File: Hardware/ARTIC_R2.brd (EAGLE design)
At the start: 22.9 x 50.8 mm, 96 parts, among them J1 U.FL, J2 THING_PLUS, Q1 20V/4.2A/52mΩ/1.4W, U1 32M SPI Flash, U2 1.8V/100mA, U3 ARTIC_R2, U4 RFPA0133, U5 AS179-92LF, U6 DUAL-OPTOISOLATOR_SOIC8, X1 CRYSTAL-TCXO-26MHZ

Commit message: Nearing completion
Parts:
- added D3: RED, SparkFun-LED:LED-0603
- added JP5: JUMPER-SMT_2_NC_TRACE_SILK, SparkFun-Jumpers:SMT-JUMPER_2_NC_TRACE_SILK
- added R15: 1k, SparkFun-Resistors:0402-TIGHT
- added SPARKX1, SPARKX2: SPARKX-LOGO4, SparkX:SPARKX-MEDIUM
- added U$1: (no value), output:#TX#0
- added U$10: (no value), output:#CIPO0
- added U$11: (no value), output:#COPI0
- added U$12: (no value), output:COPI#0
- added U$13: (no value), output:#SCLK0
- added U$14: (no value), output:SCLK#0
- added U$15: (no value), output:#CS0
- added U$16: (no value), output:CS#0
- added U$17: (no value), output:GND#0
- added U$18: (no value), output:#RESETB0
- added U$19: (no value), output:#PWR_EN0
- added U$2: (no value), output:#RX#0
- added U$20: (no value), output:G8#0
- added U$21: (no value), output:#G80
- added U$22: (no value), output:G16#0
- added U$23: (no value), output:#G160
- added U$24: (no value), output:#BOOT0
- added U$25: (no value), output:#INT10
- added U$26: (no value), output:#INT20
- added U$27: (no value), output:#PWR_LED#0
- added U$28: (no value), output:#PWR#0
- added U$29: (no value), output:ARTIC_R2_BREAKOUT0
- added U$3: (no value), output:#RX_LED#0
- added U$4: (no value), output:#TX_LED#0
- added U$5, U$6: (no value), output:#3#3V#0
- added U$7, U$8: (no value), output:#1#8V#0
- added U$9: (no value), output:CIPO#0
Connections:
- new net N$37: D3.A, R15.1
- new net N$38: D3.C, JP5.2
- net BOOT: now also J2.5
- net G16: now also J2.4
- net G8: now also J2.3
- net GND: now also JP5.1
- net INT1: now also J2.6
- net INT2: now also J2.7
- net PWR_EN: now also J2.9
- net RESETB: now also J2.8
- net VDD: now also R15.2
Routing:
- net PWR_EN: track 1.41 -> 26.5 mm
- net BOOT: track 3.34 -> 23.2 mm, vias 0 -> 1
- net INT1: track 1.59 -> 19.9 mm
- net INT2: track 0.82 -> 18.0 mm
- net RESETB: track 3.62 -> 18.3 mm, vias 0 -> 1
- net G16: track 0.00 -> 6.88 mm
- net G8: track 0.00 -> 6.41 mm
- net N$37: track 0.00 -> 5.35 mm, vias 0 -> 2
- net N$38: track 0.00 -> 2.54 mm, vias 0 -> 1
- net GND: track 77.1 -> 79.4 mm, vias 166 -> 168
- net VDD: track 82.0 -> 83.6 mm
- net PA_PD: track 26.1 -> 26.9 mm
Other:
- board text added: "15"
- board text added: "2"
- board text added: "BOT"
- board text added: "TOP"
- board text added: "X01"

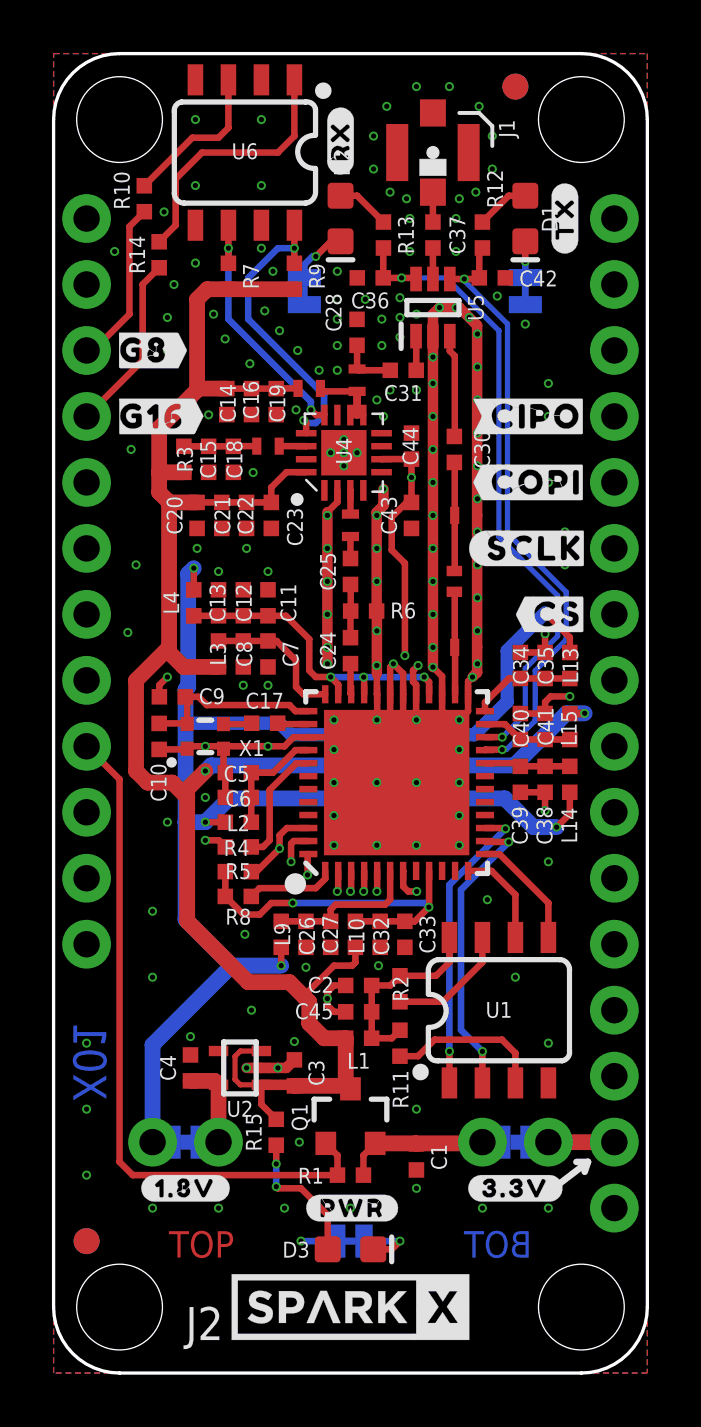
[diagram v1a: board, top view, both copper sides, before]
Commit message: Adjusted the RF track widths
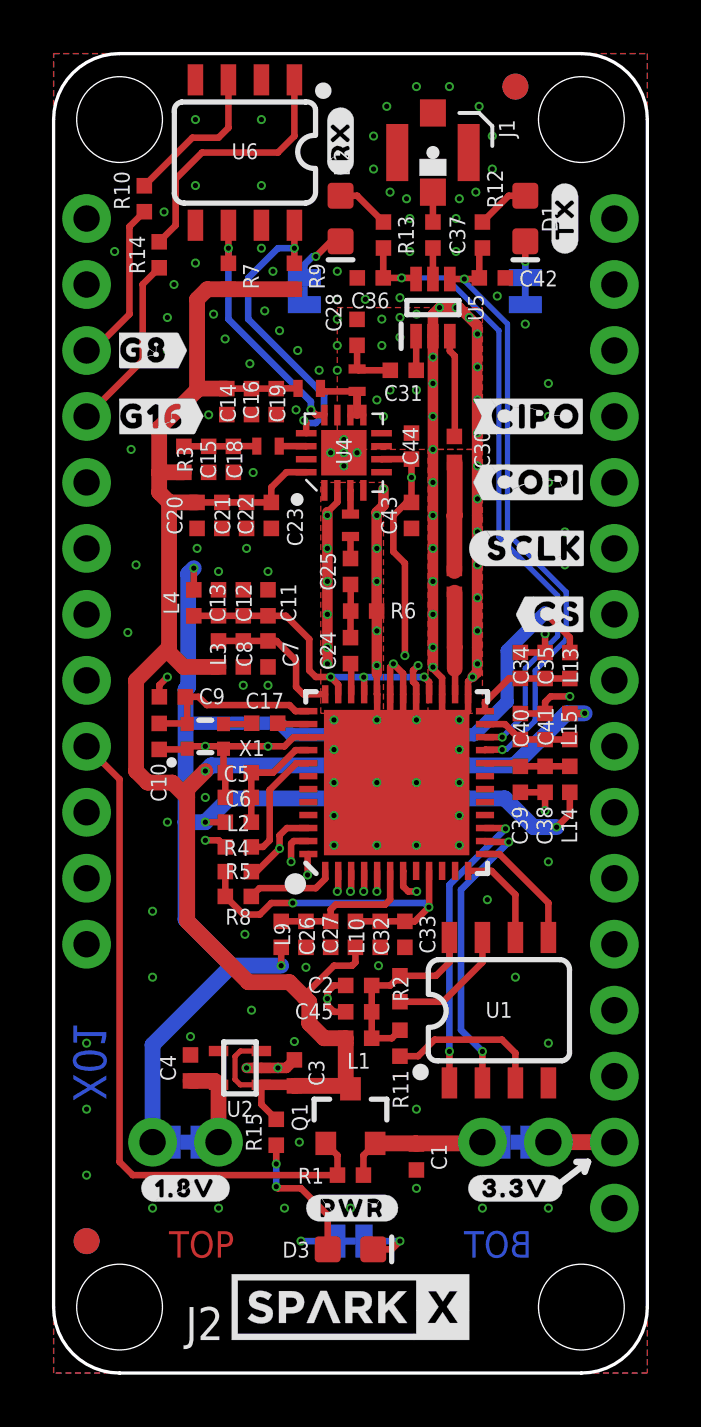
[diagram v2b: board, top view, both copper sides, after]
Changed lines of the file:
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@@
 <text x="13.97" y="4.445" size="1.016" layer="15" ratio="15">15</text>
 <text x="18.415" y="4.445" size="1.016" layer="16" ratio="15" rot="MR0">BOT</text>
+<wire x1="11.303" y1="32.639" x2="11.557" y2="32.639" width="0.254" layer="41"/>
 </plain>
 <attributes>
@@
 </element>
 <element name="X1" library="New_Parts_Clocks" package="CRYSTAL-TCXO-SMD-1.65X1.25" value="CRYSTAL-TCXO-26MHZ" x="5.842" y="24.511" smashed="yes">
+<attribute name="MOUSER_PART" value="449-LFTCXO073004CUTT" x="5.842" y="24.511" size="1.778" layer="27" display="off"/>
 <attribute name="NAME" x="7.128" y="23.756" size="0.6096" layer="25" font="vector" ratio="20"/>
+<attribute name="PROD_ID" value="" x="5.842" y="24.511" size="1.778" layer="27" display="off"/>
 </element>
 <element name="C9" library="SparkFun-Capacitors" package="0402-TIGHT" value="1.0uF" x="4.572" y="26.035" smashed="yes" rot="R180">
@@
 </element>
 <element name="R6" library="New_Parts_Resistors" package="0402-TIGHT" value="220OHM" x="11.938" y="29.337" smashed="yes" rot="R180">
+<attribute name="MOUSER_PART" value="755-SFR01MZPF2200" x="11.938" y="29.337" size="1.778" layer="27" rot="R180" display="off"/>
 <attribute name="NAME" x="13.462" y="29.664" size="0.6096" layer="25" font="vector" ratio="20" rot="R180" align="bottom-center"/>
 <attribute name="PROD_ID" value="" x="11.938" y="29.337" size="1.778" layer="27" rot="R180" display="off"/>
@@
 </element>
 <element name="R3" library="New_Parts_Resistors" package="0402-TIGHT" value="3.9OHM" x="5.0165" y="35.179" smashed="yes" rot="R270">
+<attribute name="MOUSER_PART" value="603-RC0402FR-073R9L" x="5.0165" y="35.179" size="1.778" layer="27" rot="R270" display="off"/>
 <attribute name="NAME" x="4.753" y="35.179" size="0.6096" layer="25" font="vector" ratio="20" rot="R270" align="bottom-center"/>
 <attribute name="PROD_ID" value="" x="5.0165" y="35.179" size="1.778" layer="27" ratio="15" rot="R270" display="off"/>
@@
 <contactref element="C38" pad="2"/>
 <via x="16.129" y="26.797" extent="1-16" drill="0.2"/>
-<wire x1="14.958" y1="26.133" x2="14.958" y2="26.825" width="0.254" layer="1"/>
+<wire x1="14.958" y1="26.133" x2="14.958" y2="26.7615" width="0.254" layer="1"/>
 <wire x1="14.605" y1="27.178" x2="14.605" y2="39.921" width="0.4064" layer="1"/>
-<wire x1="14.958" y1="26.825" x2="14.605" y2="27.178" width="0.254" layer="1"/>
+<wire x1="14.958" y1="26.7615" x2="14.605" y2="27.1145" width="0.254" layer="1"/>
+<wire x1="14.605" y1="27.1145" x2="14.605" y2="27.178" width="0.254" layer="1"/>
 <via x="14.605" y="27.178" extent="1-16" drill="0.2"/>
 <via x="14.605" y="31.75" extent="1-16" drill="0.2"/>
@@
 <vertex x="14.859" y="27.178"/>
 </polygon>
-<polygon width="0.254" layer="1" isolate="0.3048">
+<polygon width="0.254" layer="1" isolate="0.254" rank="3">
 <vertex x="0" y="50.8"/>
 <vertex x="22.86" y="50.8"/>
@@
 <vertex x="0" y="0"/>
 </polygon>
-<polygon width="0.254" layer="2" isolate="0.3048">
+<polygon width="0.254" layer="2" isolate="0.254" rank="2">
 <vertex x="0" y="50.8"/>
 <vertex x="22.86" y="50.8"/>
@@
 <vertex x="0" y="0"/>
 </polygon>
-<polygon width="0.254" layer="15" isolate="0.3048">
+<polygon width="0.254" layer="15" isolate="0.254" rank="2">
 <vertex x="0" y="50.8"/>
 <vertex x="22.86" y="50.8"/>
@@
 <vertex x="0" y="0"/>
 </polygon>
-<polygon width="0.254" layer="16" isolate="0.3048">
+<polygon width="0.254" layer="16" isolate="0.254" rank="2">
 <vertex x="0" y="50.8"/>
 <vertex x="22.86" y="50.8"/>
@@
 <wire x1="10.9093" y1="5.08" x2="9.525" y2="5.08" width="0.254" layer="16"/>
 <via x="9.525" y="5.08" extent="1-16" drill="0.2"/>
+<polygon width="0.1524" layer="1" isolate="0.127">
+<vertex x="10.287" y="34.29"/>
+<vertex x="12.7" y="34.29"/>
+<vertex x="12.7" y="25.4"/>
+<vertex x="10.287" y="25.4"/>
+</polygon>
+<polygon width="0.1524" layer="1" isolate="0.0762" rank="2">
+<vertex x="14.4145" y="35.56"/>
+<vertex x="16.51" y="35.56"/>
+<vertex x="16.51" y="25.4"/>
+<vertex x="14.4145" y="25.4"/>
+</polygon>
+<polygon width="0.1524" layer="1" isolate="0.127">
+<vertex x="10.922" y="41.021"/>
+<vertex x="16.51" y="41.021"/>
+<vertex x="16.51" y="35.56"/>
+<vertex x="10.922" y="35.56"/>
+</polygon>
 </signal>
 <signal name="EDAP">
@@
 <contactref element="C29" pad="P$2"/>
 <contactref element="L12" pad="P$2"/>
-<wire x1="15.4432" y1="33.02" x2="15.4432" y2="30.8927" width="0.254" layer="1"/>
 <wire x1="15.4432" y1="30.8927" x2="15.4305" y2="30.88" width="0.254" layer="1"/>
-<wire x1="15.4432" y1="33.02" x2="15.4432" y2="35.0473" width="0.254" layer="1"/>
 <wire x1="15.4432" y1="35.0473" x2="15.4305" y2="35.06" width="0.254" layer="1"/>
+<wire x1="15.4305" y1="30.88" x2="15.4305" y2="33.0073" width="0.6096" layer="1"/>
+<wire x1="15.4305" y1="33.0073" x2="15.4432" y2="33.02" width="0.6096" layer="1"/>
+<wire x1="15.4432" y1="33.02" x2="15.4432" y2="35.0473" width="0.6096" layer="1"/>
 </signal>
 <signal name="ANTENNA">
@@
 <wire x1="13.7795" y1="33.52" x2="13.7795" y2="34.4805" width="0.254" layer="1"/>
 <wire x1="13.7795" y1="33.52" x2="13.589" y2="33.52" width="0.254" layer="1"/>
-<wire x1="13.589" y1="33.52" x2="13.0175" y2="32.9485" width="0.254" layer="1"/>
+<wire x1="13.589" y1="33.52" x2="13.081" y2="33.012" width="0.254" layer="1"/>
 <wire x1="13.5255" y1="31.1785" x2="13.5255" y2="27.6225" width="0.254" layer="1"/>
 <via x="13.5255" y="27.6225" extent="1-16" drill="0.2"/>
-<wire x1="13.0175" y1="32.9485" x2="13.0175" y2="31.6865" width="0.254" layer="1"/>
-<wire x1="13.0175" y1="31.6865" x2="13.5255" y2="31.1785" width="0.254" layer="1"/>
+<wire x1="13.081" y1="33.012" x2="13.081" y2="31.623" width="0.254" layer="1"/>
+<wire x1="13.081" y1="31.623" x2="13.5255" y2="31.1785" width="0.254" layer="1"/>
 <wire x1="13.5255" y1="27.6225" x2="13.5255" y2="22.225" width="0.2032" layer="15"/>
-<wire x1="13.5255" y1="22.225" x2="12.1285" y2="20.828" width="0.2032" layer="15"/>
+<wire x1="13.5255" y1="22.225" x2="12.0015" y2="20.701" width="0.2032" layer="15"/>
 <wire x1="10.4775" y1="18.034" x2="11.43" y2="17.0815" width="0.2032" layer="15"/>
 <wire x1="11.43" y1="17.0815" x2="13.1445" y2="17.0815" width="0.2032" layer="15"/>
@@
 <wire x1="13.9795" y1="17.9165" x2="13.9795" y2="18.542" width="0.2032" layer="15"/>
 <wire x1="13.1445" y1="17.0815" x2="13.9795" y2="17.9165" width="0.2032" layer="15"/>
-<wire x1="12.1285" y1="20.828" x2="12.0015" y2="20.701" width="0.2032" layer="15"/>
 <wire x1="12.0015" y1="19.2405" x2="11.7475" y2="18.9865" width="0.2032" layer="15"/>
 <wire x1="10.7315" y1="18.9865" x2="10.4775" y2="18.7325" width="0.2032" layer="15"/>
@@
 <contactref element="U3" pad="34"/>
 <contactref element="C24" pad="1"/>
-<wire x1="11.458" y1="26.133" x2="11.43" y2="26.161" width="0.254" layer="1"/>
-<wire x1="11.43" y1="26.161" x2="11.43" y2="27.313" width="0.254" layer="1"/>
+<wire x1="11.458" y1="26.133" x2="11.458" y2="27.285" width="0.254" layer="1"/>
+<wire x1="11.458" y1="27.285" x2="11.43" y2="27.313" width="0.254" layer="1"/>
 </signal>
 <signal name="N$18">
@@
 <contactref element="L11" pad="P$2"/>
 <contactref element="C29" pad="P$1"/>
-<wire x1="15.458" y1="26.133" x2="15.458" y2="27.9252" width="0.254" layer="1"/>
+<wire x1="15.4432" y1="30.0673" x2="15.4305" y2="30.08" width="0.254" layer="1"/>
+<wire x1="15.4305" y1="30.0546" x2="15.4432" y2="30.0673" width="0.254" layer="1"/>
 <wire x1="15.458" y1="27.9252" x2="15.4432" y2="27.94" width="0.254" layer="1"/>
-<wire x1="15.4432" y1="27.94" x2="15.4432" y2="30.0673" width="0.254" layer="1"/>
-<wire x1="15.4432" y1="30.0673" x2="15.4305" y2="30.08" width="0.254" layer="1"/>
+<wire x1="15.4432" y1="30.0419" x2="15.44005" y2="30.04505" width="0.254" layer="1"/>
+<wire x1="15.44005" y1="30.04505" x2="15.4305" y2="30.0546" width="0.254" layer="1"/>
+<wire x1="15.4432" y1="27.94" x2="15.44005" y2="27.94760625" width="0.254" layer="1" curve="-45"/>
+<wire x1="15.4432" y1="27.1145" x2="15.4432" y2="27.94" width="0.6096" layer="1"/>
+<wire x1="15.458" y1="26.133" x2="15.458" y2="27.0997" width="0.254" layer="1"/>
+<wire x1="15.458" y1="27.0997" x2="15.4432" y2="27.1145" width="0.254" layer="1"/>
+<wire x1="15.44005" y1="27.94760625" x2="15.44005" y2="30.04505" width="0.6096" layer="1"/>
 </signal>
 <signal name="N$22">

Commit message: Added 4x4 test panel
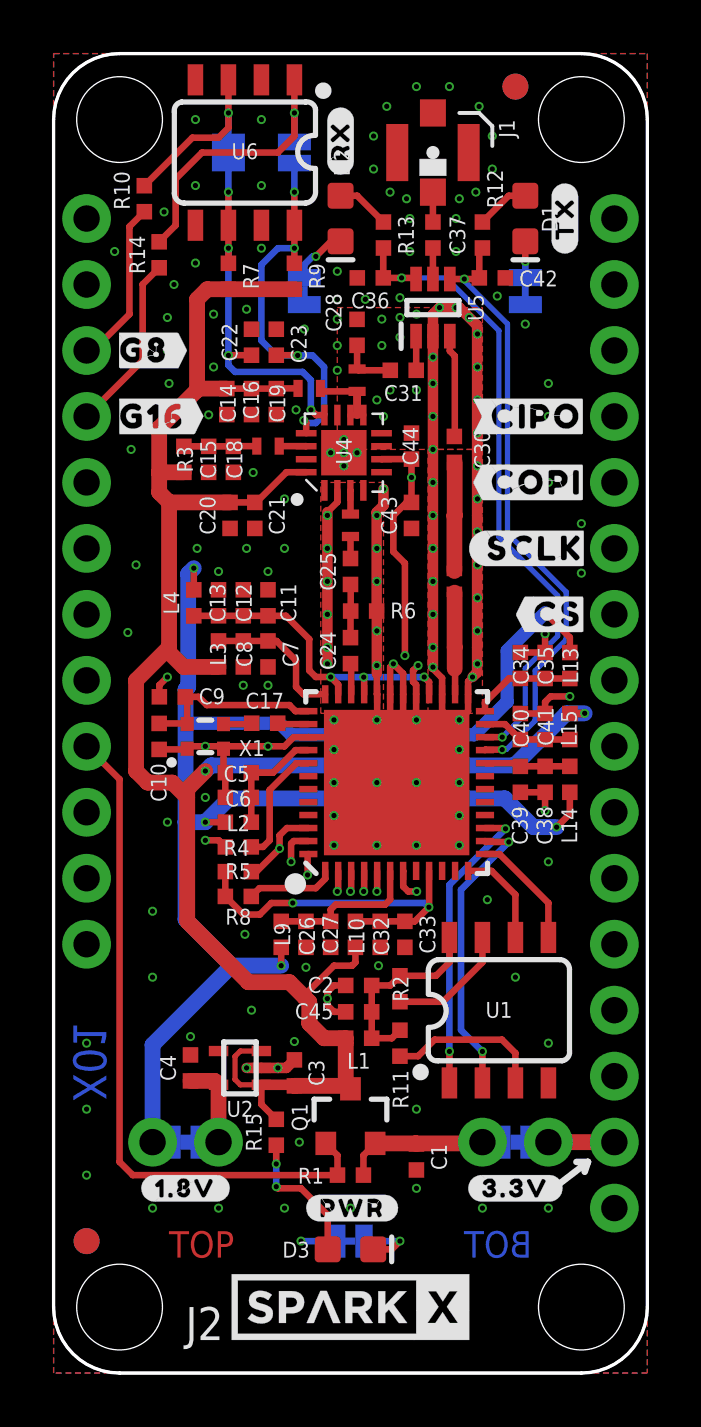
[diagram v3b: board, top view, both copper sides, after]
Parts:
- added JP6, JP7: JUMPER-SMT_2_NO_SILK, SparkFun-Jumpers:SMT-JUMPER_2_NO_SILK
- moved C22 6.67 mm to (7.62, 39.7), turned to 270 degrees
- moved C23 6.67 mm to (8.57, 39.7), turned to 270 degrees
- moved C20 1.27 mm to (6.79, 33.0)
- moved C21 1.27 mm to (7.75, 33.0)
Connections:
- removed net N$33: R9.1, U4.13, U6.8
- removed net N$34: R7.1, U4.12, U6.6
- new net RFG16: C23.2, JP6.2, R9.1, U4.13, U6.8
- new net RFG8: C22.2, JP7.2, R7.1, U4.12, U6.6
- net N$23: now also JP7.1
- net N$27: now also JP6.1
- net VDD: no longer C22.2, C23.2
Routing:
- net RFG16: track 0.00 -> 15.3 mm, vias 0 -> 4
- net RFG8: track 0.00 -> 14.4 mm, vias 0 -> 4
- net N$33: track 11.7 -> 0.00 mm, vias 2 -> 0
- net N$34: track 9.60 -> 0.00 mm, vias 2 -> 0
- net N$27: track 10.1 -> 11.2 mm, vias 0 -> 1
- net N$23: track 6.01 -> 7.13 mm, vias 0 -> 1
- net CIPO: track 24.2 -> 23.5 mm
- net SCLK: track 21.9 -> 21.4 mm
- net GND: vias 168 -> 167

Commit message: ).8mm PCB with Impedance Control
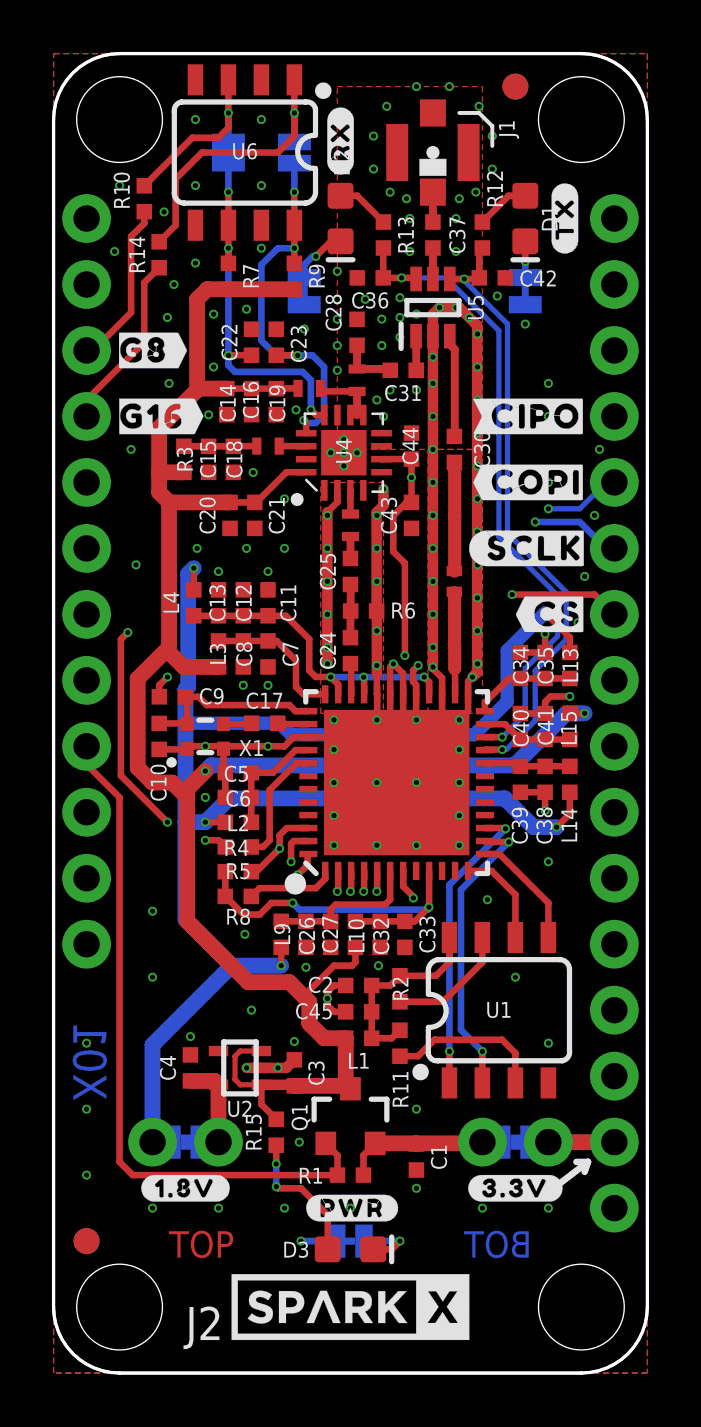
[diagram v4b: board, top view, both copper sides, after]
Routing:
- net GND: track 79.4 -> 87.5 mm, vias 167 -> 171
- net SCLK: track 21.4 -> 24.0 mm, vias 1 -> 2
- net PA_PD: track 26.8 -> 24.6 mm
- net CIPO: track 23.5 -> 24.1 mm
- net CS: track 21.9 -> 21.4 mm, vias 1 -> 2
- net COPI: track 22.9 -> 23.2 mm, vias 1 -> 2
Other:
- board text added: "JLCPCB JLC7628 4-Layer 0.8mm Impedance Control 4-Layer Board 0.8mm Thickness 1oz Copper (Outer layers) ENIG Finish"
- board text added: "Paul Clark"
- board text removed: "4-Layer Board 1.6mm Thickness 1oz Copper ENIG Finish"
